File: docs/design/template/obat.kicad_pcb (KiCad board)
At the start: 2 copper layers, 100 x 220 mm, 3 parts

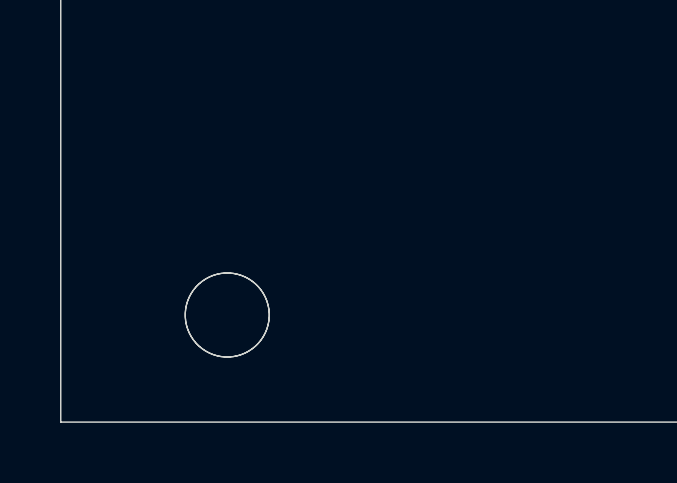
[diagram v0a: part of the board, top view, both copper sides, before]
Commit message: fix obat.kicad_pcb eurocard pcb template: duplicate mounting hole
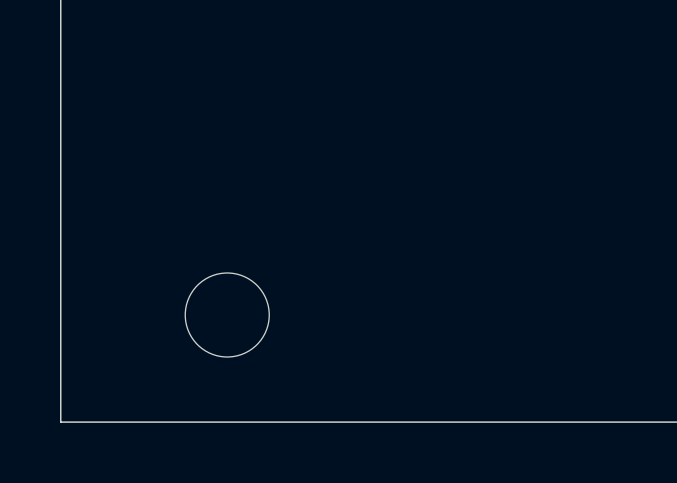
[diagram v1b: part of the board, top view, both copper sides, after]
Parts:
- removed ?: , 
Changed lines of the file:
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@@
-		)
-	)
-	(footprint ""
-		(locked yes)
-		(layer "F.Cu")
-		(at 155.55 256.43)
-		(property "Reference" ""
-			(at 0 0 0)
-			(unlocked yes)
-			(layer "F.SilkS")
-			(effects
-				(font
-					(size 1.27 1.27)
-				)
-			)
-		)
-		(property "Value" ""
-			(at 0 0 0)
-			(unlocked yes)
-			(layer "F.Fab")
-			(effects
-				(font
-					(size 1.27 1.27)
-				)
-			)
-		)
-		(property "Footprint" ""
-			(at 0 0 0)
-			(unlocked yes)
-			(layer "F.Fab")
-			(hide yes)
-			(effects
-				(font
-					(size 1.27 1.27)
-				)
-			)
-		)
-		(property "Datasheet" ""
-			(at 0 0 0)
-			(unlocked yes)
-			(layer "F.Fab")
-			(hide yes)
-			(effects
-				(font
-					(size 1.27 1.27)
-				)
-			)
-		)
-		(property "Description" ""
-			(at 0 0 0)
-			(unlocked yes)
-			(layer "F.Fab")
-			(hide yes)
-			(effects
-				(font
-					(size 1.27 1.27)
-				)
-			)
-		)
-		(pad "" np_thru_hole circle
-			(at 0 0)
-			(size 2.8 2.8)
-			(drill 2.8)
-			(layers "F&B.Cu" "*.Mask")
 		)
 	)
@@
 		(height -5)
 		(orientation 1)
-		(gr_text "3.5700 mm"
+		(gr_text "140.5512 mils"
 			(locked yes)
 			(at 145 251 90)
@@
 		(height 5)
 		(orientation 0)
-		(gr_text "88.9000 mm"
+		(gr_text "3500.0000 mils"
 			(locked yes)
 			(at 200 262.5 0)
